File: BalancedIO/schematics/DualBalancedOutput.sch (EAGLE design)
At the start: 27 parts, among them IC1 THAT1646, IC2 THAT1646, J1 CON-JST_PH_3W

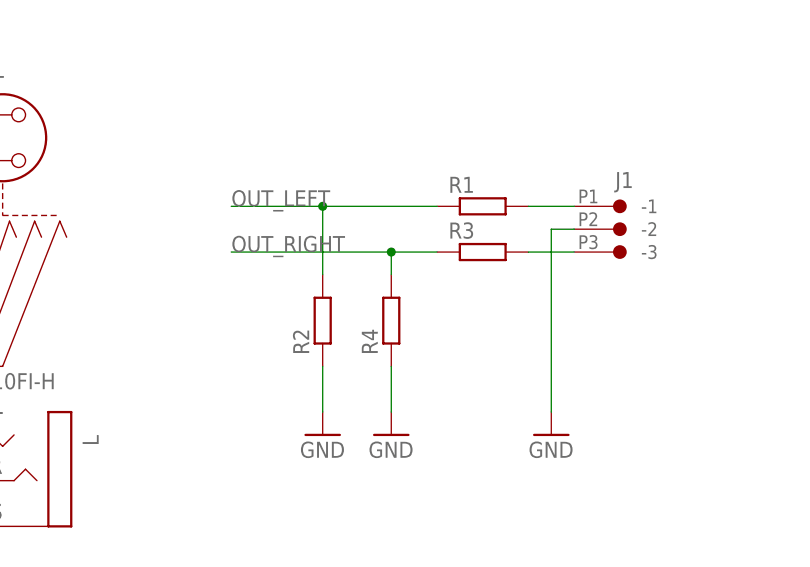
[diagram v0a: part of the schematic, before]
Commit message: set resistor values for voltage divider
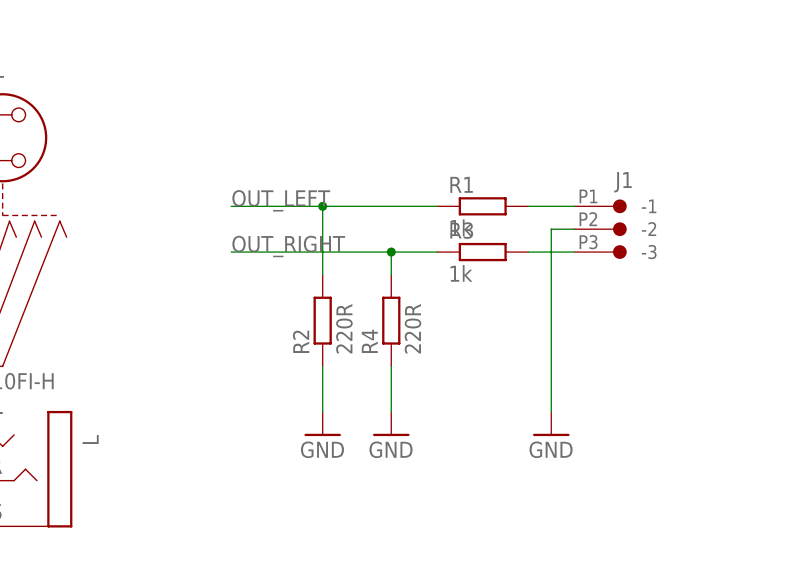
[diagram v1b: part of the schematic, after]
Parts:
- R1, R3: value (none) -> 1k
- R2, R4: value (none) -> 220R
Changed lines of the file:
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@@
 <part name="C4" library="Rebel" deviceset="CPOL-EU" device="E2-5" value="10u NP"/>
 <part name="GND4" library="supply1" deviceset="GNDA" device=""/>
-<part name="R1" library="Rebel" deviceset="R-EU_" device="0204/7"/>
-<part name="R3" library="Rebel" deviceset="R-EU_" device="0204/7"/>
-<part name="R4" library="Rebel" deviceset="R-EU_" device="0204/7"/>
-<part name="R2" library="Rebel" deviceset="R-EU_" device="0204/7"/>
+<part name="R1" library="Rebel" deviceset="R-EU_" device="0204/7" value="1k"/>
+<part name="R3" library="Rebel" deviceset="R-EU_" device="0204/7" value="1k"/>
+<part name="R4" library="Rebel" deviceset="R-EU_" device="0204/7" value="220R"/>
+<part name="R2" library="Rebel" deviceset="R-EU_" device="0204/7" value="220R"/>
 <part name="GND1" library="supply1" deviceset="GND" device=""/>
 <part name="GND13" library="supply1" deviceset="GND" device=""/>
